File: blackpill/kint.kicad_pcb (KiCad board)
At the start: 2 copper layers, 99.9 x 86 mm, 21 parts, among them J1 THUMB_RIGHT_SPC_KB600, J2 LEFT_13_LT, J3 TOP_LEFT, J4 TOP_RIGHT, J5 THUMB_LEFT_BAK, J6 THUMB_RIGHT_SPC, J7 RIGHT_13_DOWN, J8 THUMB_LEFT_BAK_KB600, U1 YAAJ_WeAct_BlackPill_Part_Lik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

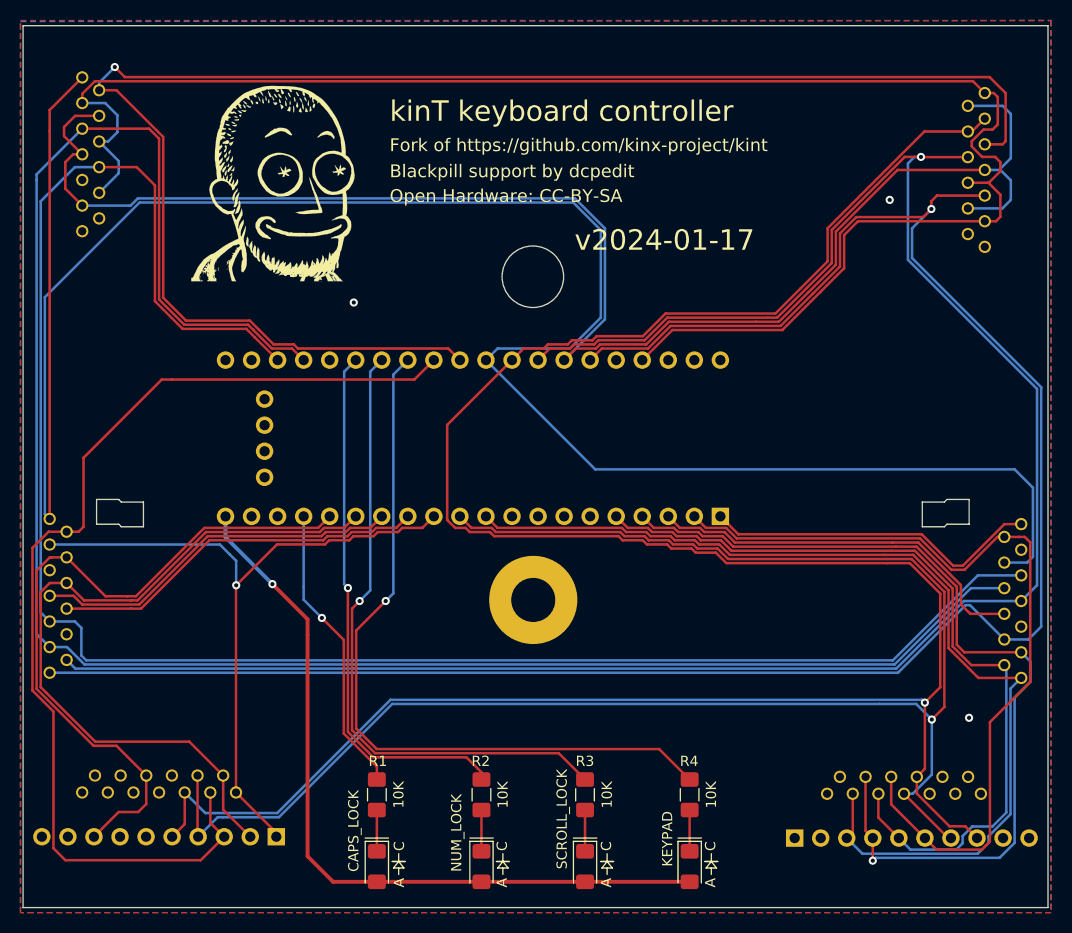
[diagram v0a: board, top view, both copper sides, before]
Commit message: remove unused KB500 connectors and move components
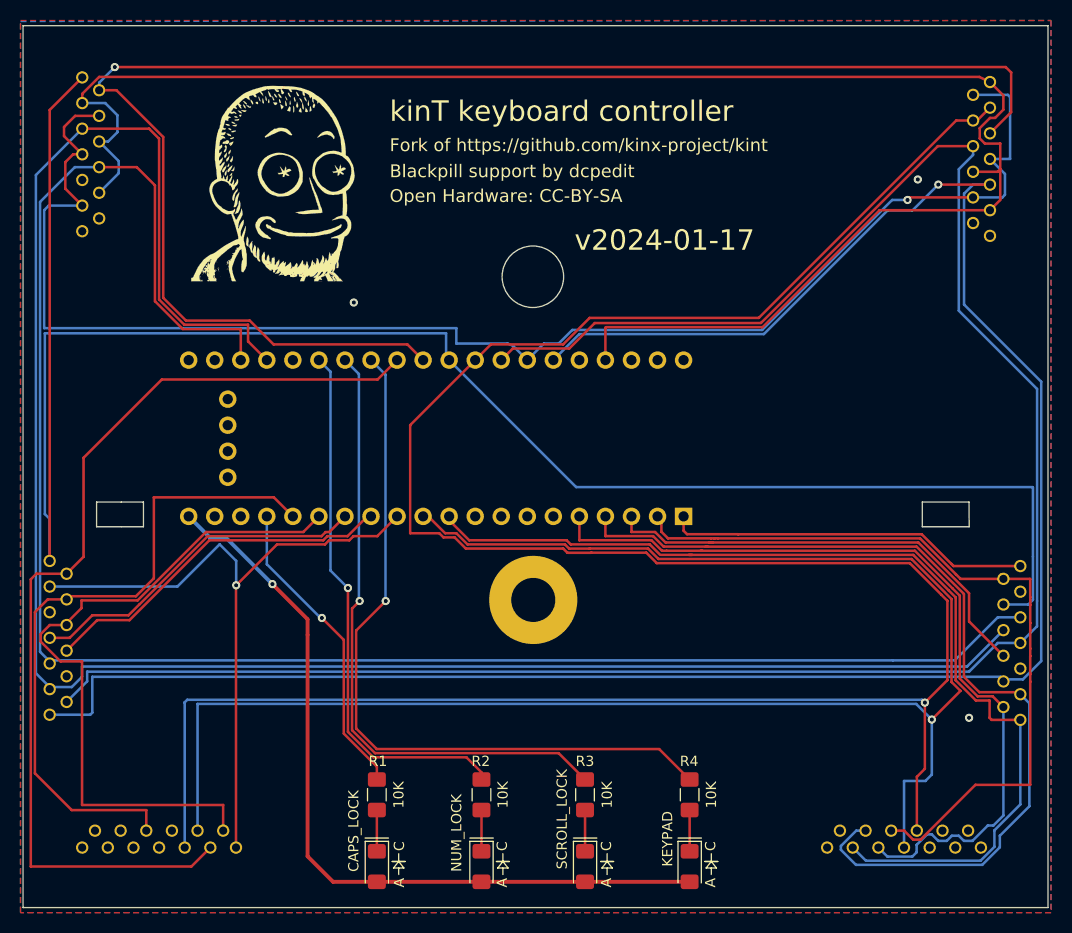
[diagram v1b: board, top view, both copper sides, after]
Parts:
- removed J5: THUMB_LEFT_BAK, Connector_PinHeader_2.54mm:PinHeader_1x10_P2.54mm_Vertical
- removed J6: THUMB_RIGHT_SPC, Connector_PinHeader_2.54mm:PinHeader_1x10_P2.54mm_Vertical
- moved J8 5.37 mm to (112.0, 142.2)
- moved J1 5.25 mm to (184.7, 142.2)
- moved J2 4.10 mm to (101.3, 121.7)
- moved J7 4.09 mm to (196.0, 122.2)
- moved U1 3.59 mm to (163.2, 109.9)
- moved J4 1.19 mm to (193.0, 75.0)
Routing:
- net /COL_0: track 215.0 -> 188.6 mm
- net /ROW_5: track 103.8 -> 96.5 mm
- net /COL_5: track 237.7 -> 244.8 mm
- net /COL_4: track 195.5 -> 202.4 mm
- net /ROW_MIN: track 37.8 -> 44.5 mm
- net /ROW_9: track 81.7 -> 76.1 mm
- net /COL_6: track 162.0 -> 167.4 mm
- net /COL_3: track 198.3 -> 203.5 mm, vias 1 -> 0
- net /ROW_2: track 72.9 -> 68.1 mm
- net /ROW_ESC: track 152.9 -> 149.0 mm
- net /ROW_3: track 68.8 -> 65.2 mm
- net /ROW_F2: track 151.5 -> 148.2 mm, vias 0 -> 1
- net /COL_1: track 181.5 -> 178.8 mm
- net /ROW_F1: track 166.4 -> 169.1 mm
- net /ROW_0: track 33.0 -> 35.7 mm
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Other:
- outline, holes or cut-outs redrawn
- board text removed: "-or-"
- board text removed: "KB500"
- board text removed: "KB600"

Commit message: update footprint values
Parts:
- J1: value THUMB_RIGHT_SPC_KB600 -> RIGHT_THUMB
- J2: value LEFT_13_LT -> LEFT_KEYWELL
- J3: value TOP_LEFT -> LEFT_TOP
- J4: value TOP_RIGHT -> RIGHT_TOP
- J7: value RIGHT_13_DOWN -> RIGHT_KEYWELL
- J8: value THUMB_LEFT_BAK_KB600 -> LEFT_THUMB
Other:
- board text added: "WeAct STM32F4x"
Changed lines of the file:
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@@
 			)
 		)
-		(property "Value" "LEFT_13_LT"
-			(at -5.207 -5.08 90)
+		(property "Value" "LEFT_KEYWELL"
+			(at -4.7 -5.154 90)
 			(unlocked yes)
 			(layer "B.SilkS")
-			(hide yes)
 			(effects
 				(font
@@
 		)
 		(property "Datasheet" ""
-			(at 0 0 270)
+			(at 0 0 90)
 			(layer "F.Fab")
 			(hide yes)
@@
 		)
 		(property "Description" ""
-			(at 0 0 270)
+			(at 0 0 90)
 			(layer "F.Fab")
 			(hide yes)
@@
 			)
 		)
-		(property "Value" "TOP_LEFT"
-			(at -4.064 -4.953 90)
+		(property "Value" "LEFT_TOP"
+			(at -2.049 -4.953 90)
 			(unlocked yes)
 			(layer "B.SilkS")
@@
 			)
 		)
-		(property "Value" "RIGHT_13_DOWN"
-			(at 6.35 -5.08 270)
+		(property "Value" "RIGHT_KEYWELL"
+			(at 5.7 -5 270)
 			(unlocked yes)
 			(layer "B.SilkS")
@@
 			)
 		)
-		(property "Value" "TOP_RIGHT"
-			(at -3.429 -4.953 270)
+		(property "Value" "RIGHT_TOP"
+			(at -5.5 -4.953 270)
 			(unlocked yes)
 			(layer "B.SilkS")
@@
 			)
 		)
-		(property "Value" "THUMB_LEFT_BAK_KB600"
-			(at -10.16 3.81 180)
-			(layer "B.Fab")
-			(hide yes)
+		(property "Value" "LEFT_THUMB"
+			(at -5.514 -3.652 180)
+			(layer "B.SilkS")
 			(effects
 				(font
-					(size 1.6891 1.6891)
+					(size 1 1)
 					(thickness 0.135128)
 				)
@@
 			)
 		)
-		(property "Value" "THUMB_RIGHT_SPC_KB600"
-			(at -10.16 3.81 180)
-			(layer "B.Fab")
-			(hide yes)
+		(property "Value" "RIGHT_THUMB"
+			(at -4.658 -3.652 180)
+			(layer "B.SilkS")
 			(effects
 				(font
-					(size 1.6891 1.6891)
+					(size 1 1)
 					(thickness 0.135128)
 				)
@@
 		)
 	)
+	(gr_text "WeAct STM32F4x"
+		(at 111 101.5 90)
+		(layer "B.SilkS")
+		(effects
+			(font
+				(size 1 1)
+				(thickness 0.15)
+			)
+			(justify mirror)
+		)
+	)

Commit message: minor track improveents
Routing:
- net /COL_5: track 244.8 -> 258.8 mm, vias 1 -> 0
- net /COL_6: track 167.4 -> 176.5 mm, vias 1 -> 0
- net /ROW_9: track 76.1 -> 83.6 mm
- net /ROW_F1: track 169.1 -> 165.2 mm
- net /ROW_ESC: track 149.0 -> 145.5 mm, vias 1 -> 0
- net /ROW_6: track 98.4 -> 100.2 mm
- net /ROW_7: track 90.4 -> 92.0 mm
- net /ROW_8: track 81.5 -> 82.8 mm
- net /ROW_F2: track 148.2 -> 147.9 mm, vias 1 -> 0

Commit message: update attributions
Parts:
- removed G*** (x2): LOGO, kinx:logo
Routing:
- net /ROW_4: track 67.0 -> 62.3 mm
- net /ROW_3: track 65.2 -> 66.0 mm
- net /ROW_7: track 92.0 -> 92.7 mm
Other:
- board text added: "Based on kinT by Michael Stapelberg"
- board text added: "Kinesis keyboard controller"
- board text added: "v2025-05-08"
- board text removed: "Fork of https://github.com/kinx-project/kint"
- board text removed: "kinT keyboard controller"
- board text removed: "v2024-01-17"

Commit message: track cleanup
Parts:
- J3: value LEFT_TOP -> LEFT_FN_KEYS
- J4: value RIGHT_TOP -> RIGHT_FN_KEYS
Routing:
- net /COL_5: track 258.8 -> 193.5 mm, vias 0 -> 1
- net /COL_6: track 176.5 -> 113.3 mm, vias 0 -> 1
- net /ROW_F2: track 147.9 -> 198.9 mm
- net /ROW_7: track 92.7 -> 83.0 mm
- net /COL_0: track 188.6 -> 183.2 mm
- net /COL_3: track 203.5 -> 198.6 mm
- net /ROW_F1: track 165.2 -> 169.2 mm
- net /COL_4: track 202.7 -> 199.1 mm, vias 1 -> 0
- net /ROW_3: track 66.0 -> 64.1 mm
- net /ROW_4: track 62.3 -> 63.3 mm
- net /3V3: track 77.2 -> 76.2 mm
- net /ROW_9: track 83.6 -> 84.5 mm
- net /ROW_8: track 82.8 -> 83.4 mm
- net GND: vias 3 -> 0
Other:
- board text added: "Kinesis Keyboard Controller"
- board text added: "STM32F4x"
- board text added: "maso"
- board text added: "v1.0"
- board text removed: "Based on kinT by Michael Stapelberg"
- board text removed: "Blackpill support by dcpedit"
- board text removed: "Kinesis keyboard controller"
- board text removed: "Molex 39-53-2135"
- board text removed: "WeAct STM32F4x"
- board text removed: "v2025-05-08"

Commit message: tracks
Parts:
- moved J2 0.65 mm to (102.0, 121.7)
- moved J7 0.50 mm to (195.5, 122.2)
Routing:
- net /COL_5: track 193.5 -> 252.3 mm
- net /COL_3: track 198.6 -> 246.3 mm
- net /COL_4: track 199.1 -> 222.5 mm
- net /COL_1: track 178.5 -> 162.3 mm
- net /ROW_F2: track 198.9 -> 184.0 mm
- net /ROW_ESC: track 146.0 -> 132.2 mm
- net /ROW_F1: track 169.2 -> 178.8 mm
- net /ROW_7: track 83.0 -> 75.2 mm
- net /ROW_8: track 83.4 -> 76.4 mm
- net /ROW_3: track 64.1 -> 57.7 mm, vias 0 -> 1
- net /ROW_2: track 67.7 -> 61.4 mm, vias 0 -> 1
- net /ROW_5: track 96.5 -> 102.5 mm
- net /ROW_6: track 100.5 -> 95.4 mm
- net /ROW_MIN: track 44.9 -> 41.4 mm
- net /COL_0: track 183.2 -> 180.3 mm
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- removed copper zone on F.Cu, net GND

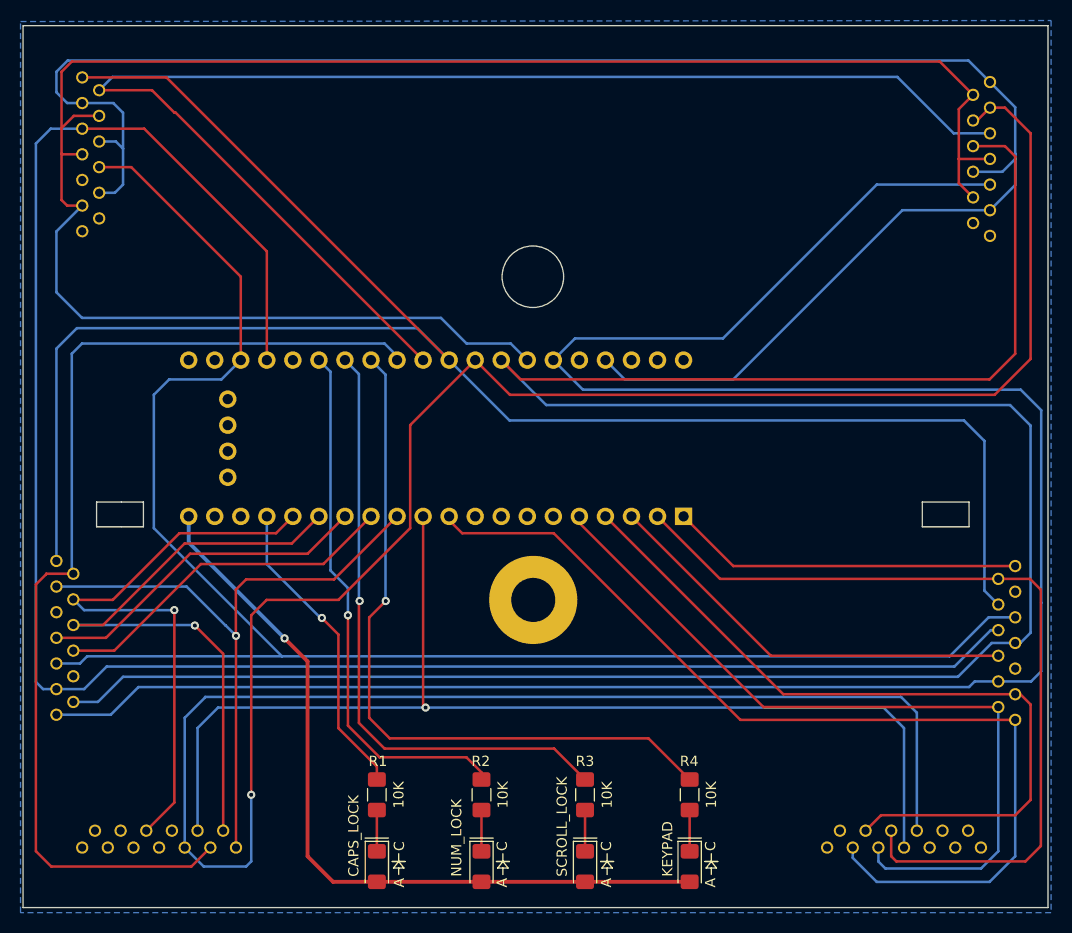
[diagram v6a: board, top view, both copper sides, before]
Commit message: fix fill zone
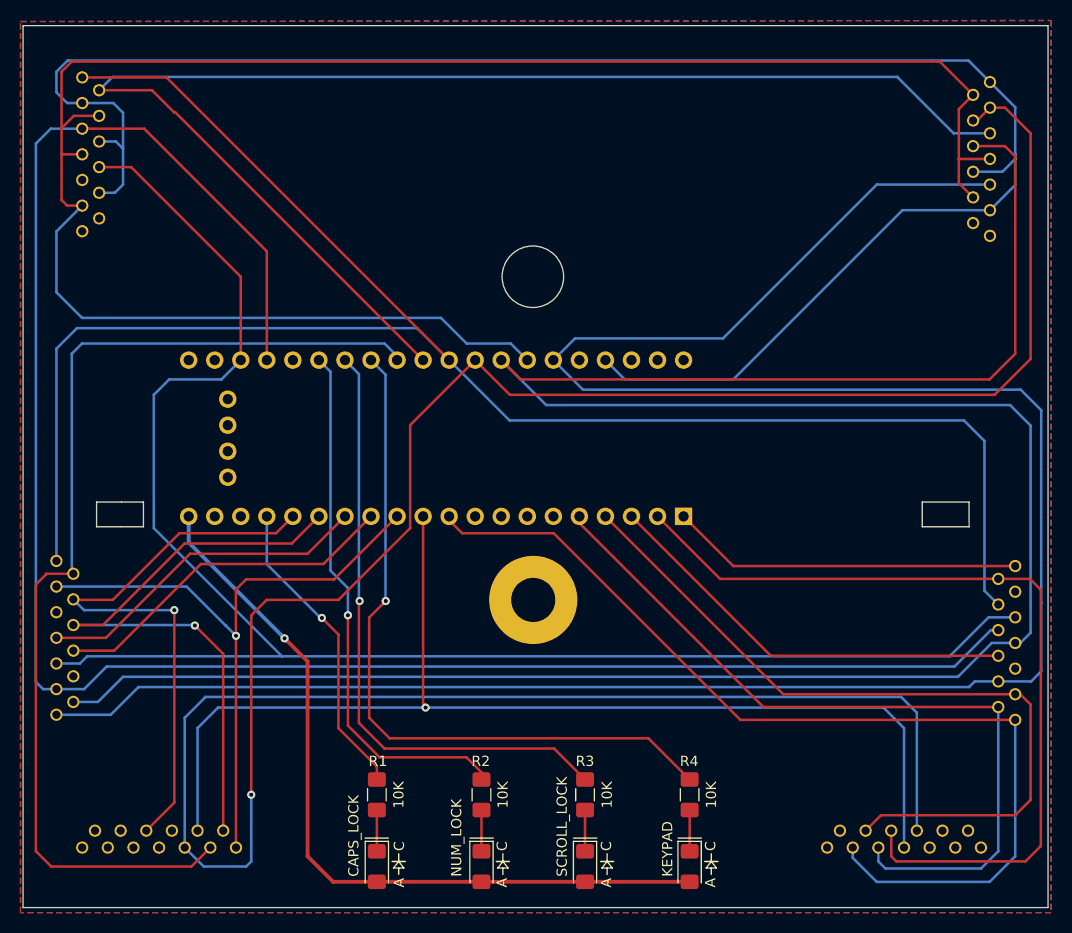
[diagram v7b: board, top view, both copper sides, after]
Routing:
- added copper zone on F.Cu, net GND
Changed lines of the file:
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@@
 		(net 31)
 		(net_name "GND")
-		(layer "B.Cu")
+		(layers "F.Cu" "B.Cu")
 		(hatch edge 0.508)
 		(priority 6)

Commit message: Move thumb connectors for less strain on ribbon cables
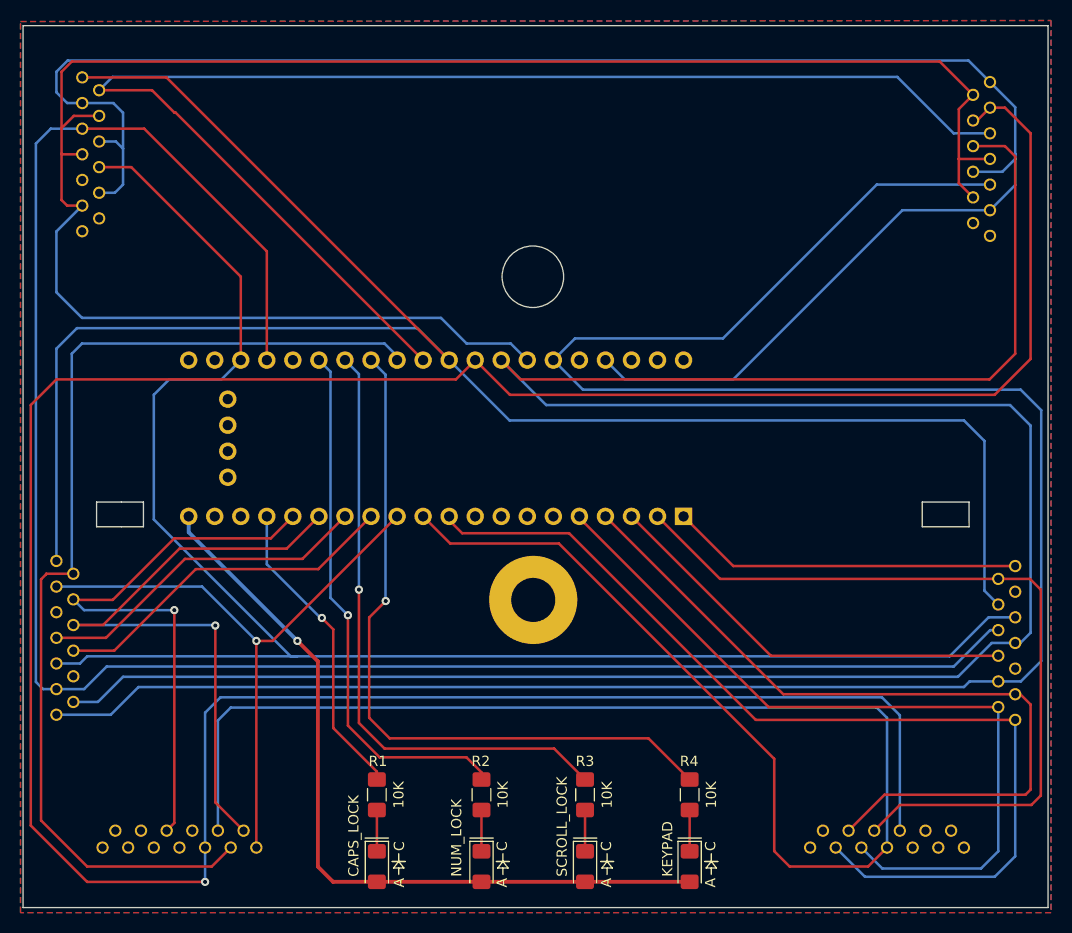
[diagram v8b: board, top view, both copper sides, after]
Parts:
- moved J8 1.99 mm to (114.0, 142.2)
- moved J1 1.66 mm to (183.0, 142.2)
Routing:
- net /COL_6: track 110.9 -> 155.0 mm, vias 1 -> 0
- net /COL_5: track 252.3 -> 288.1 mm
- net /ROW_9: track 82.8 -> 77.6 mm
- net /ROW_4: track 63.3 -> 60.6 mm
- net /ROW_2: track 61.4 -> 63.3 mm
- net /ROW_7: track 75.2 -> 76.3 mm
- net /COL_1: track 162.3 -> 163.3 mm
- net /ROW_8: track 76.4 -> 77.2 mm
- net /ROW_3: track 57.7 -> 56.8 mm
- net /ROW_6: track 95.4 -> 96.1 mm
- net /COL_4: track 222.5 -> 221.9 mm
- net /COL_2: track 188.2 -> 187.7 mm
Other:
- board text added: "v1.1"
- board text removed: "v1.0"
